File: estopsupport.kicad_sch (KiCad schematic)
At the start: 25 parts, among them J1 ESTOP1, J2 ESTOP2, J3 CONTACTOR, J4 TAP_ESTOP, J5 5V_IN, J6 PWR, U1 PC817, U2 BTS6163D

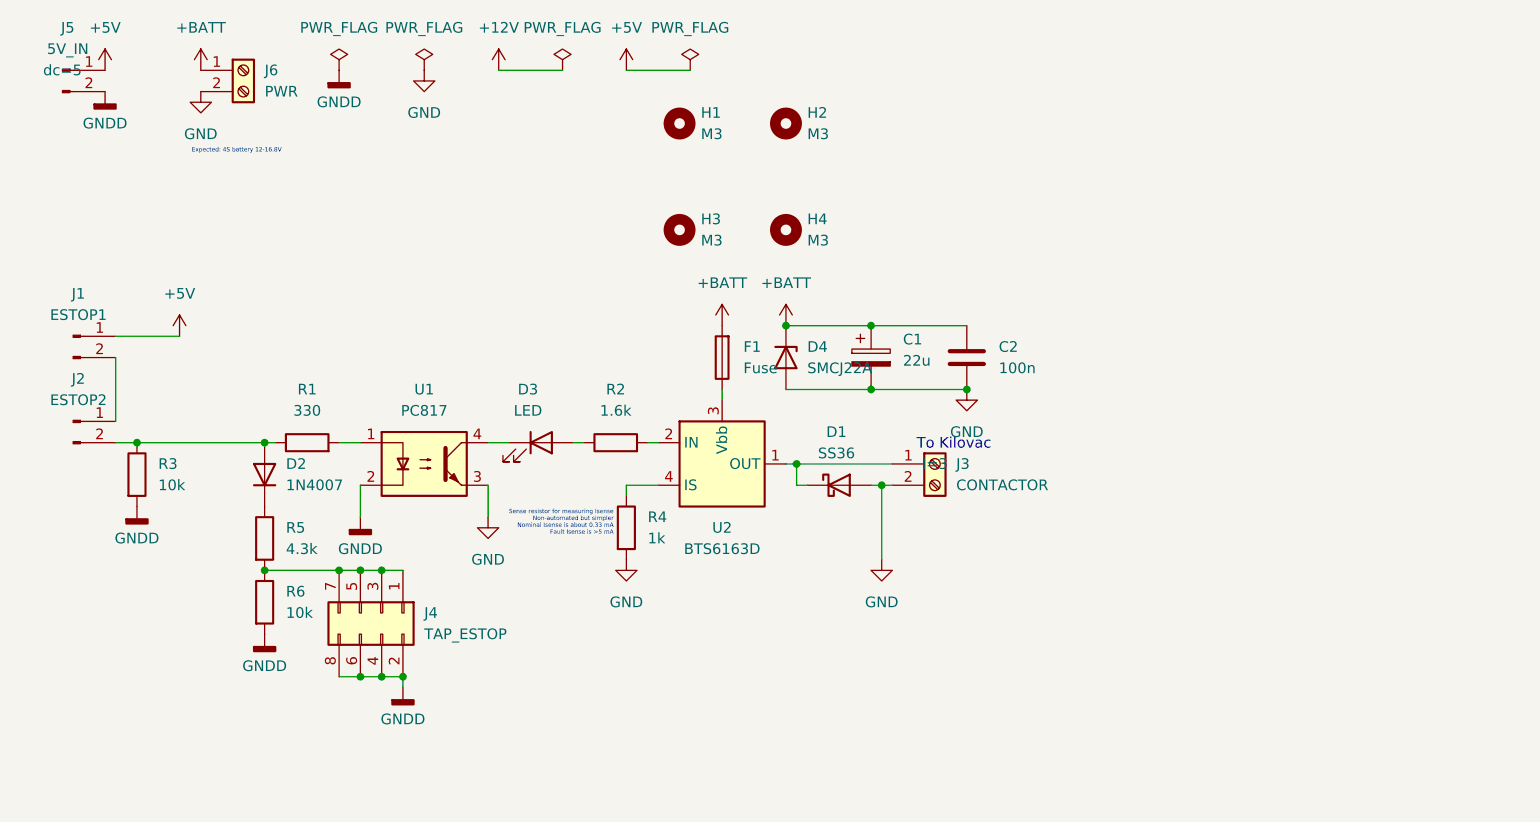
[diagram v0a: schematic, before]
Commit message: feat: include logo properly, reroute to use capacitors properly, add fuse
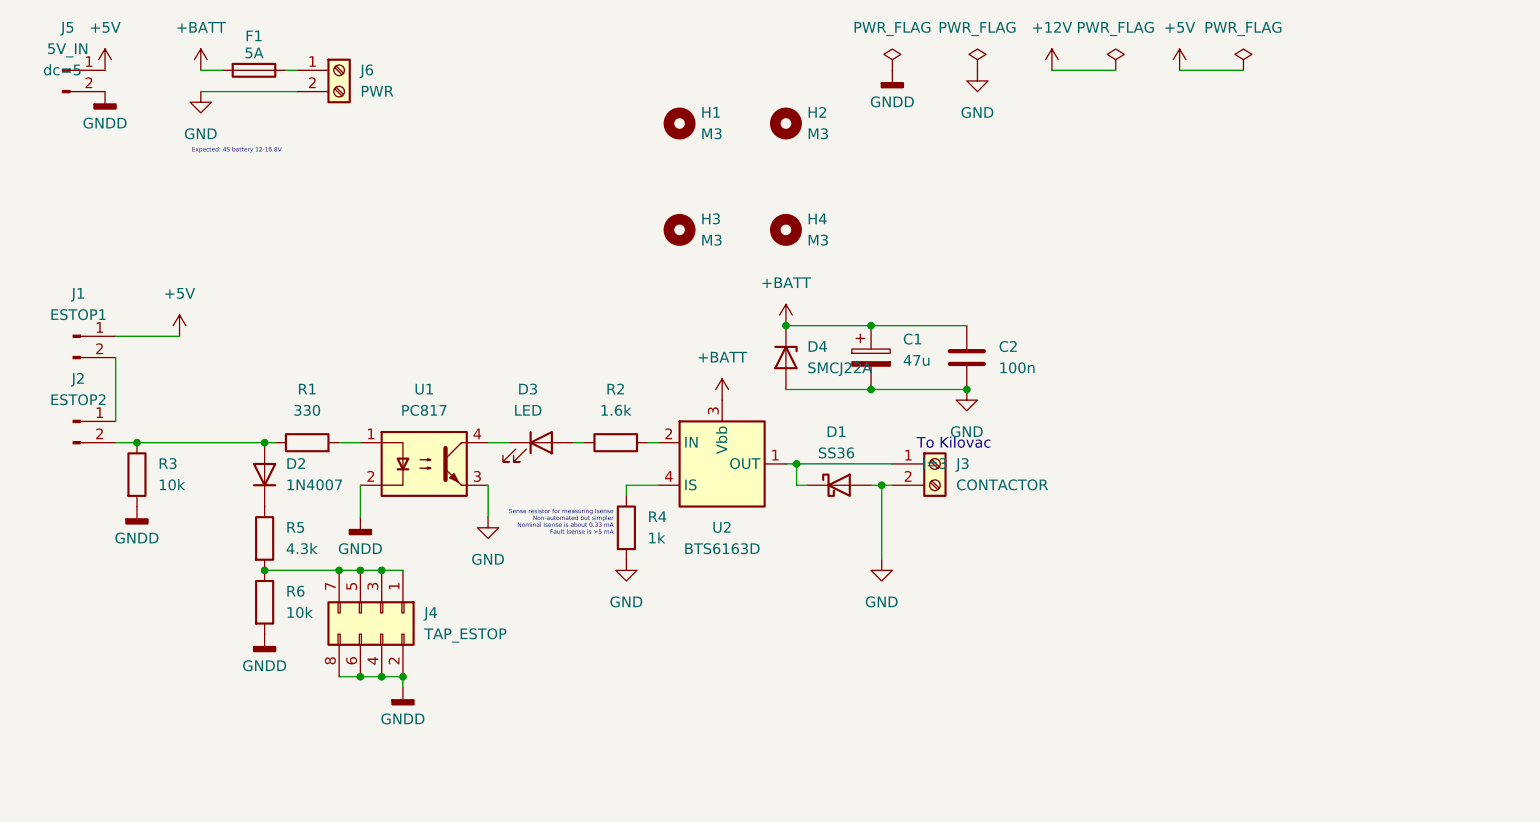
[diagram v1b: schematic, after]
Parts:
- C1: value 22u -> 47u; footprint Capacitor_SMD:CP_Elec_4x5.4 -> Capacitor_SMD:CP_Elec_6.3x5.4
- F1: value Fuse -> 5A
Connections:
- net +BATT: now also U2.3 (Vbb); no longer J6.1 (Pin_1)
- net at F1.1: now also J6.1 (Pin_1); no longer U2.3 (Vbb)
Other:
- moved on the sheet: F1, J6

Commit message: fix: remove unneeded flyback for kilovac major rearrangement
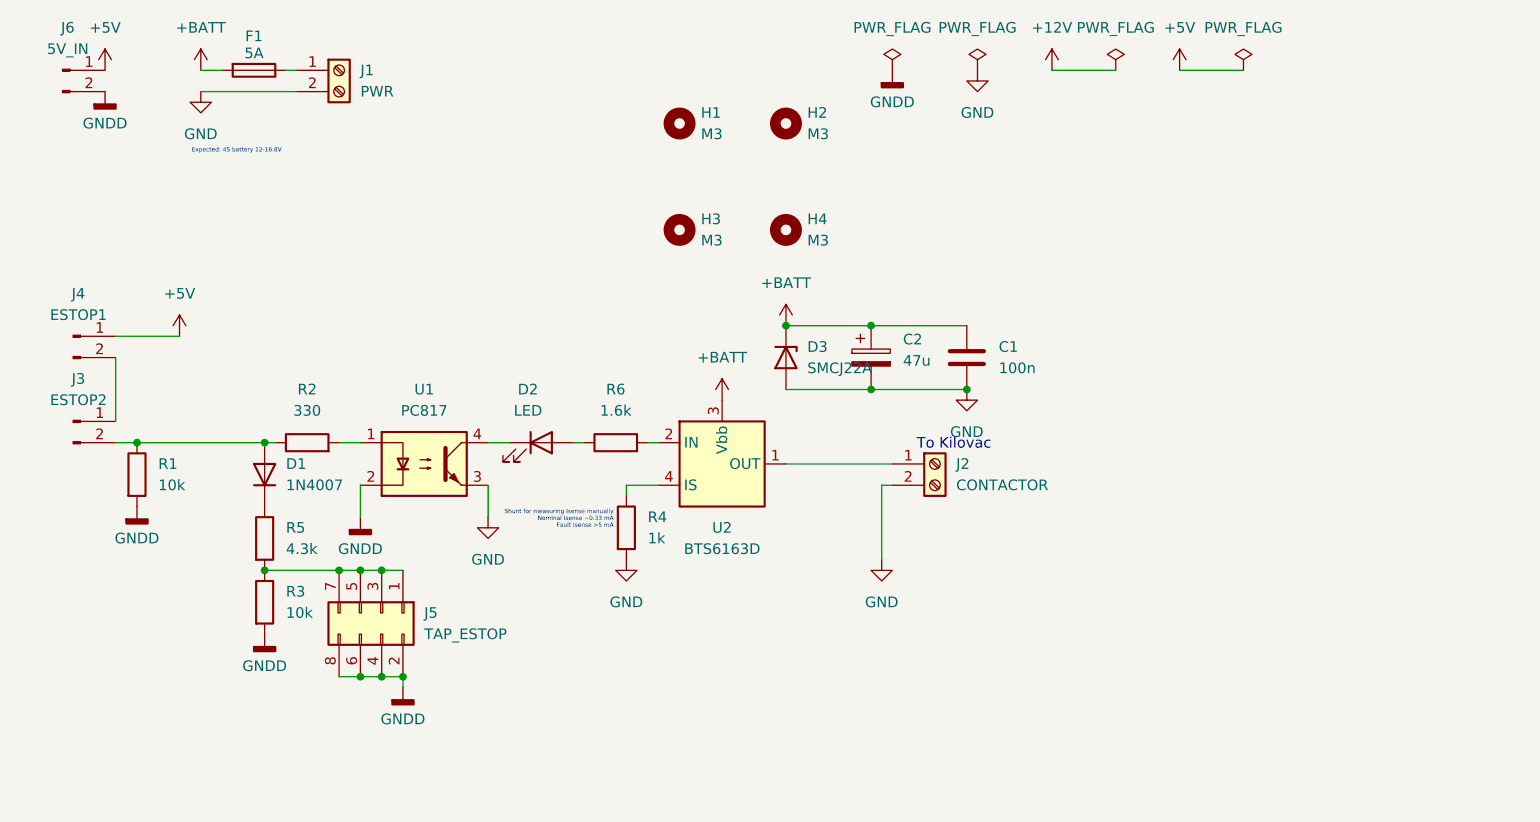
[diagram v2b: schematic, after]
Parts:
- removed D1: SS36, Diode_SMD:D_SMA, symbol Diode:SS36
- renumbered C2 to C1, C1 to C2, D2 to D1, D3 to D2, D4 to D3, J6 to J1, J3 to J2, J2 to J3, J1 to J4, J4 to J5, J5 to J6, R3 to R1, R1 to R2, R6 to R3, R2 to R6
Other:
- note added: "Shunt for measuring Isense manually Nominal Isense ~0.33 mA Fault Isense >5 mA"
- note removed: "Sense resistor for measuring Isense Non-automated but simpler Nominal Isense is about 0.33 mA Fault Isense is >5 mA"
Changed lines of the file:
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@@
 		(comment 2 "Designed to operate a Kilovac using 2 5V switches in series")
 	)
-	(text "Sense resistor for measuring Isense\nNon-automated but simpler\nNominal Isense is about 0.33 mA\nFault Isense is >5 mA"
+	(text "Shunt for measuring Isense manually\nNominal Isense ~0.33 mA\nFault Isense >5 mA"
 		(exclude_from_sim no)
 		(at 81.026 71.628 0)
@@
 	)
 	(junction
-		(at 113.03 68.58)
-		(diameter 0)
-		(color 0 0 0 0)
-	)
-	(junction
 		(at 111.76 57.15)
 		(diameter 0)
@@
 	)
 	(junction
-		(at 102.87 66.04)
-		(diameter 0)
-		(color 0 0 0 0)
-	)
-	(junction
 		(at 53.34 78.74)
 		(diameter 0)
@@
 	(wire
 		(pts
-			(xy 111.76 68.58) (xy 113.03 68.58)
-		)
-		(stroke
-			(width 0)
-			(type default)
-		)
-	)
-	(wire
-		(pts
-			(xy 102.87 68.58) (xy 104.14 68.58)
-		)
-		(stroke
-			(width 0)
-			(type default)
-		)
-	)
-	(wire
-		(pts
 			(xy 21.59 63.5) (xy 24.13 63.5)
 		)
@@
 	(wire
 		(pts
-			(xy 102.87 66.04) (xy 102.87 68.58)
-		)
-		(stroke
-			(width 0)
-			(type default)
-		)
-	)
-	(wire
-		(pts
 			(xy 21.59 53.34) (xy 21.59 60.96)
 		)
@@
 	(wire
 		(pts
-			(xy 102.87 66.04) (xy 114.3 66.04)
-		)
-		(stroke
-			(width 0)
-			(type default)
-		)
-	)
-	(wire
-		(pts
 			(xy 76.2 63.5) (xy 77.47 63.5)
 		)
@@
 	(wire
 		(pts
-			(xy 101.6 66.04) (xy 102.87 66.04)
+			(xy 101.6 66.04) (xy 114.3 66.04)
 		)
 		(stroke
@@
 		(dnp no)
 		(fields_autoplaced yes)
-		(property "Reference" "C2"
+		(property "Reference" "C1"
 			(at 127 52.0699 0)
 			(show_name no)
@@
 			(project "estopsupport"
 				(path "/ca51e45a-2cf8-42c4-bf53-5bd38d2544be"
-					(reference "C2")
+					(reference "C1")
 					(unit 1)
 				)
@@
 	)
 	(symbol
-		(lib_id "Diode:SS36")
-		(at 107.95 68.58 0)
-		(unit 1)
-		(body_style 1)
-		(exclude_from_sim no)
-		(in_bom yes)
-		(on_board yes)
-		(in_pos_files yes)
-		(dnp no)
-		(fields_autoplaced yes)
-		(property "Reference" "D1"
-			(at 107.6325 62.23 0)
-			(show_name no)
-			(do_not_autoplace no)
-			(effects
-				(font
-					(size 1.27 1.27)
-				)
-			)
-		)
-		(property "Value" "SS36"
-			(at 107.6325 64.77 0)
-			(show_name no)
-			(do_not_autoplace no)
-			(effects
-				(font
-					(size 1.27 1.27)
-				)
-			)
-		)
-		(property "Footprint" "Diode_SMD:D_SMA"
-			(at 107.95 73.025 0)
-			(hide yes)
-			(show_name no)
-			(do_not_autoplace no)
-			(effects
-				(font
-					(size 1.27 1.27)
-				)
-			)
-		)
-		(property "Datasheet" "https://www.vishay.com/docs/88751/ss32.pdf"
-			(at 107.95 68.58 0)
-			(hide yes)
-			(show_name no)
-			(do_not_autoplace no)
-			(effects
-				(font
-					(size 1.27 1.27)
-				)
-			)
-		)
-		(property "Description" "60V 3A Schottky Diode, SMA"
-			(at 107.95 68.58 0)
-			(hide yes)
-			(show_name no)
-			(do_not_autoplace no)
-			(effects
-				(font
-					(size 1.27 1.27)
-				)
-			)
-		)
-		(property "Sim.Device" "D"
-			(at 107.95 68.58 0)
-			(hide yes)
-			(show_name no)
-			(do_not_autoplace no)
-			(effects
-				(font
-					(size 1.27 1.27)
-				)
-			)
-		)
-		(property "Sim.Pins" "1=K 2=A"
-			(at 107.95 68.58 0)
-			(hide yes)
-			(show_name no)
-			(do_not_autoplace no)
-			(effects
-				(font
-					(size 1.27 1.27)
-				)
-			)
-		)
-		(property "JLCPCB Part #" "C16015"
-			(at 107.95 68.58 0)
-			(hide yes)
-			(show_name no)
-			(do_not_autoplace no)
-			(effects
-				(font
-					(size 1.27 1.27)
-				)
-			)
-		)
-		(pin "1"
-		)
-		(pin "2"
-		)
-		(instances
-			(project "estopsupport"
-				(path "/ca51e45a-2cf8-42c4-bf53-5bd38d2544be"
-					(reference "D1")
-					(unit 1)
-				)
-			)
-		)
-	)
-	(symbol
 		(lib_id "Power_Management:BTS6163D")
 		(at 93.98 66.04 0)
@@
 		(dnp no)
 		(fields_autoplaced yes)
-		(property "Reference" "J6"
+		(property "Reference" "J1"
 			(at 50.8 19.0499 0)
 			(show_name no)
@@
 			(project "estopsupport"
 				(path "/ca51e45a-2cf8-42c4-bf53-5bd38d2544be"
-					(reference "J6")
+					(reference "J1")
 					(unit 1)
 				)
@@
 		(dnp no)
 		(fields_autoplaced yes)
-		(property "Reference" "D4"
+		(property "Reference" "D3"
 			(at 104.14 52.0699 90)
 			(show_name no)
@@
 			(project "estopsupport"
 				(path "/ca51e45a-2cf8-42c4-bf53-5bd38d2544be"
-					(reference "D4")
+					(reference "D3")
 					(unit 1)
 				)
@@
 		(dnp no)
 		(fields_autoplaced yes)
-		(property "Reference" "R3"
+		(property "Reference" "R1"
 			(at 26.67 66.0399 0)
 			(show_name no)
@@
 			(project "estopsupport"
 				(path "/ca51e45a-2cf8-42c4-bf53-5bd38d2544be"
-					(reference "R3")
+					(reference "R1")
 					(unit 1)
 				)
@@
 		(dnp no)
 		(fields_autoplaced yes)
-		(property "Reference" "J2"
+		(property "Reference" "J3"
 			(at 17.145 55.88 0)
 			(show_name no)
@@
 			(project "estopsupport"
 				(path "/ca51e45a-2cf8-42c4-bf53-5bd38d2544be"
-					(reference "J2")
+					(reference "J3")
 					(unit 1)
 				)
@@
 		(dnp no)
 		(fields_autoplaced yes)
-		(property "Reference" "C1"
+		(property "Reference" "C2"
 			(at 115.57 51.1809 0)
 			(show_name no)
@@
 			(project "estopsupport"
 				(path "/ca51e45a-2cf8-42c4-bf53-5bd38d2544be"
-					(reference "C1")
+					(reference "C2")
 					(unit 1)
 				)
@@
 		(dnp no)
 		(fields_autoplaced yes)
-		(property "Reference" "D2"
+		(property "Reference" "D1"
 			(at 41.91 66.0399 90)
 			(show_name no)
@@
 			(project "estopsupport"
 				(path "/ca51e45a-2cf8-42c4-bf53-5bd38d2544be"
-					(reference "D2")
+					(reference "D1")
 					(unit 1)
 				)
@@
 		(dnp no)
 		(fields_autoplaced yes)
-		(property "Reference" "R6"
+		(property "Reference" "R3"
 			(at 41.91 81.2799 0)
 			(show_name no)
@@
 			(project "estopsupport"
 				(path "/ca51e45a-2cf8-42c4-bf53-5bd38d2544be"
-					(reference "R6")
+					(reference "R3")
 					(unit 1)
 				)
@@
 		(dnp no)
 		(fields_autoplaced yes)
-		(property "Reference" "J3"
+		(property "Reference" "J2"
 			(at 121.92 66.0399 0)
 			(show_name no)
@@
 		(property "Sim.Params" "l=3"
 			(at 119.38 66.04 0)
+			(hide yes)
 			(show_name no)
 			(do_not_autoplace no)
@@
 			(project "estopsupport"
 				(path "/ca51e45a-2cf8-42c4-bf53-5bd38d2544be"
-					(reference "J3")
+					(reference "J2")
 					(unit 1)
 				)
@@
 		(dnp no)
 		(fields_autoplaced yes)
-		(property "Reference" "R2"
+		(property "Reference" "R6"
 			(at 81.28 57.15 90)
 			(show_name no)
@@
 			(project "estopsupport"
 				(path "/ca51e45a-2cf8-42c4-bf53-5bd38d2544be"
-					(reference "R2")
+					(reference "R6")
 					(unit 1)
 				)
@@
 		(dnp no)
 		(fields_autoplaced yes)
-		(property "Reference" "D3"
+		(property "Reference" "D2"
 			(at 70.8025 57.15 0)
 			(show_name no)
@@
 			(project "estopsupport"
 				(path "/ca51e45a-2cf8-42c4-bf53-5bd38d2544be"
-					(reference "D3")
+					(reference "D2")
 					(unit 1)
 				)
@@
 		(dnp no)
 		(fields_autoplaced yes)
-		(property "Reference" "J5"
+		(property "Reference" "J6"
 			(at 15.875 13.97 0)
 			(show_name no)
@@
 		(property "Sim.Params" "dc=5"
 			(at 15.24 19.05 0)
+			(hide yes)
 			(show_name no)
 			(do_not_autoplace no)
@@
 			(project "estopsupport"
 				(path "/ca51e45a-2cf8-42c4-bf53-5bd38d2544be"
-					(reference "J5")
+					(reference "J6")
 					(unit 1)
 				)
@@
 		(dnp no)
 		(fields_autoplaced yes)
-		(property "Reference" "J1"
+		(property "Reference" "J4"
 			(at 17.145 45.72 0)
 			(show_name no)
@@
 			(project "estopsupport"
 				(path "/ca51e45a-2cf8-42c4-bf53-5bd38d2544be"
-					(reference "J1")
+					(reference "J4")
 					(unit 1)
 				)
@@
 		(dnp no)
 		(fields_autoplaced yes)
-		(property "Reference" "J4"
+		(property "Reference" "J5"
 			(at 58.42 83.8199 90)
 			(show_name no)
@@
 			(project "estopsupport"
 				(path "/ca51e45a-2cf8-42c4-bf53-5bd38d2544be"
-					(reference "J4")
+					(reference "J5")
 					(unit 1)
 				)
@@
 		(dnp no)
 		(fields_autoplaced yes)
-		(property "Reference" "R1"
+		(property "Reference" "R2"
 			(at 44.45 57.15 90)
 			(show_name no)
@@
 			(project "estopsupport"
 				(path "/ca51e45a-2cf8-42c4-bf53-5bd38d2544be"
-					(reference "R1")
+					(reference "R2")
 					(unit 1)
 				)
